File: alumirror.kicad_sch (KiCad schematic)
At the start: 71 parts, among them J1 USB_C_Receptacle_USB2.0_16P_2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, J2 USB_C_Receptacle_USB2.0_16P_2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, SW00 PG1350, SW01 PG1350, SW02 PG1350, SW03 PG1350, SW04 PG1350, SW05 PG1350, SW10 PG1350, SW11 PG1350, SW12 PG1350, SW13 PG1350, SW14 PG1350, SW15 PG1350, SW20 PG1350, SW21 PG1350, SW22 PG1350, SW23 PG1350, SW24 PG1350, SW25 PG1350_1½U, SW30 PG1350_1½U, SW31 PG1350/SKQUCAA010, SW6 BOOT, U1 CH552T, U2 CH552T, U3 USBLC6-2P6, U4 USBLC6-2P6

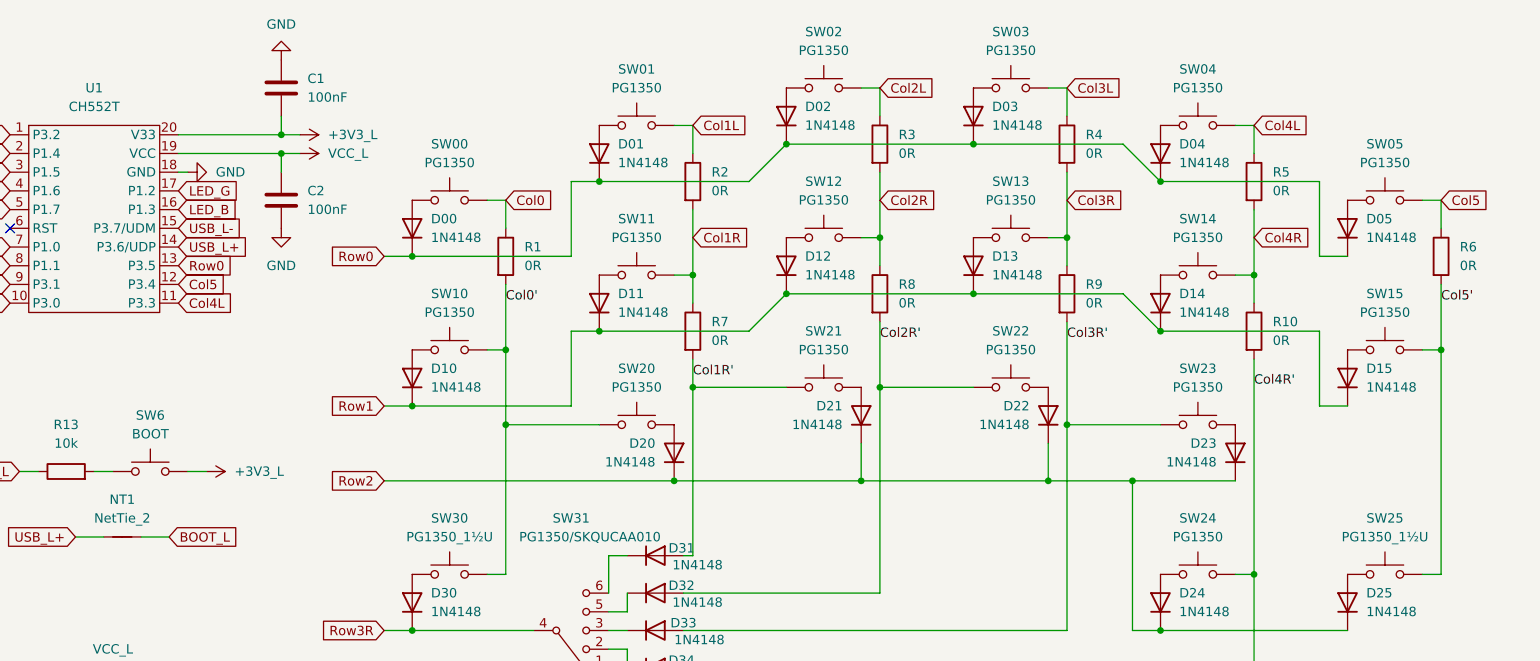
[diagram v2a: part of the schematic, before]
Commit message: Renamed all key switches to K##
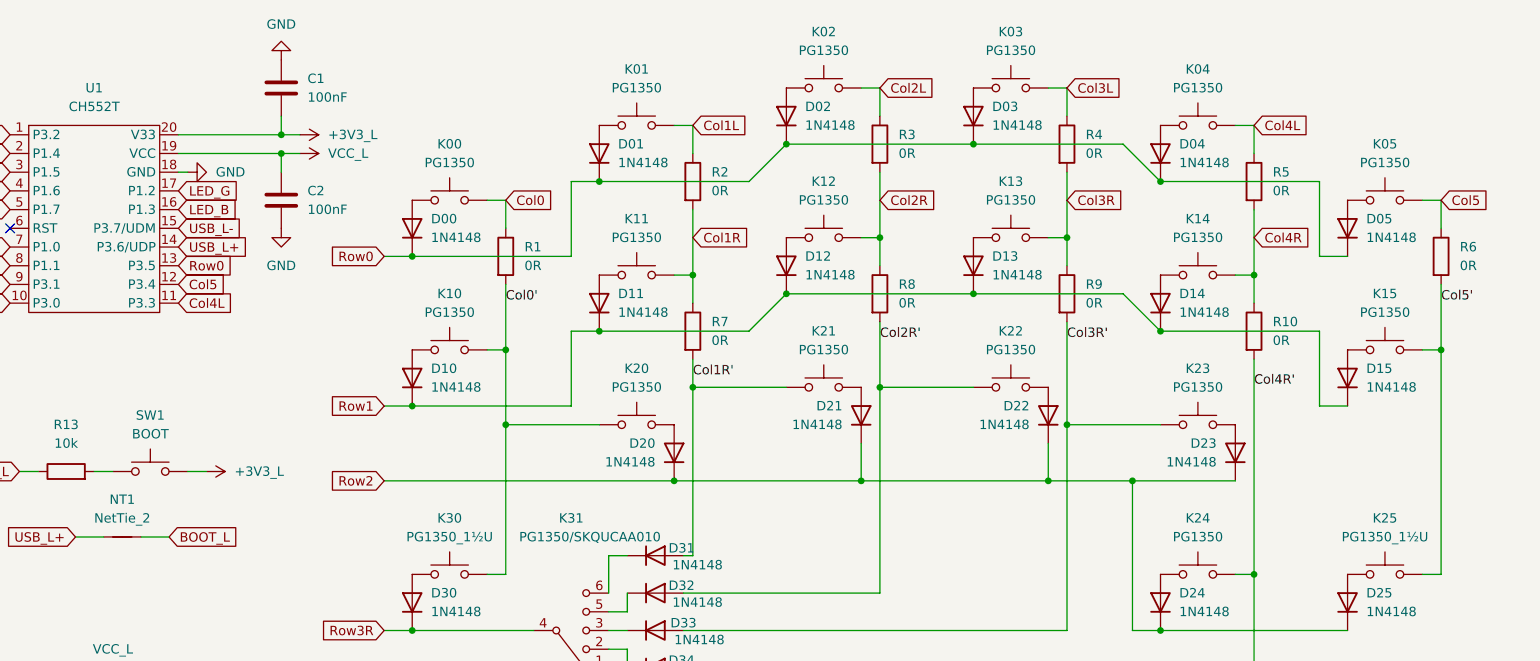
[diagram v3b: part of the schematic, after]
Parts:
- renumbered SW00 to K00, SW01 to K01, SW02 to K02, SW03 to K03, SW04 to K04, SW05 to K05, SW10 to K10, SW11 to K11, SW12 to K12, SW13 to K13, SW14 to K14, SW15 to K15, SW20 to K20, SW21 to K21, SW22 to K22, SW23 to K23, SW24 to K24, SW25 to K25, SW30 to K30, SW31 to K31, SW6 to SW1
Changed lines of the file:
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@@
 		(on_board yes)
 		(dnp no)
-		(property "Reference" "SW20"
+		(property "Reference" "K20"
 			(at 110.49 67.31 0)
 			(effects
@@
 			(project ""
 				(path "/52f043ac-ccff-4c85-bc10-2db9d3c9e3f3"
-					(reference "SW20")
+					(reference "K20")
 					(unit 1)
 				)
@@
 		(on_board yes)
 		(dnp no)
-		(property "Reference" "SW24"
+		(property "Reference" "K24"
 			(at 186.69 87.63 0)
 			(effects
@@
 			(project ""
 				(path "/52f043ac-ccff-4c85-bc10-2db9d3c9e3f3"
-					(reference "SW24")
+					(reference "K24")
 					(unit 1)
 				)
@@
 		(on_board yes)
 		(dnp no)
-		(property "Reference" "SW14"
+		(property "Reference" "K14"
 			(at 186.69 46.99 0)
 			(effects
@@
 			(project ""
 				(path "/52f043ac-ccff-4c85-bc10-2db9d3c9e3f3"
-					(reference "SW14")
+					(reference "K14")
 					(unit 1)
 				)
@@
 		(on_board yes)
 		(dnp no)
-		(property "Reference" "SW15"
+		(property "Reference" "K15"
 			(at 212.09 57.15 0)
 			(effects
@@
 			(project ""
 				(path "/52f043ac-ccff-4c85-bc10-2db9d3c9e3f3"
-					(reference "SW15")
+					(reference "K15")
 					(unit 1)
 				)
@@
 		(on_board yes)
 		(dnp no)
-		(property "Reference" "SW00"
+		(property "Reference" "K00"
 			(at 85.09 36.83 0)
 			(effects
@@
 			(project ""
 				(path "/52f043ac-ccff-4c85-bc10-2db9d3c9e3f3"
-					(reference "SW00")
+					(reference "K00")
 					(unit 1)
 				)
@@
 		(on_board yes)
 		(dnp no)
-		(property "Reference" "SW01"
+		(property "Reference" "K01"
 			(at 110.49 26.67 0)
 			(effects
@@
 			(project ""
 				(path "/52f043ac-ccff-4c85-bc10-2db9d3c9e3f3"
-					(reference "SW01")
+					(reference "K01")
 					(unit 1)
 				)
@@
 		(on_board yes)
 		(dnp no)
-		(property "Reference" "SW03"
+		(property "Reference" "K03"
 			(at 161.29 21.59 0)
 			(effects
@@
 			(project ""
 				(path "/52f043ac-ccff-4c85-bc10-2db9d3c9e3f3"
-					(reference "SW03")
+					(reference "K03")
 					(unit 1)
 				)
@@
 		(on_board yes)
 		(dnp no)
-		(property "Reference" "SW05"
+		(property "Reference" "K05"
 			(at 212.09 36.83 0)
 			(effects
@@
 			(project ""
 				(path "/52f043ac-ccff-4c85-bc10-2db9d3c9e3f3"
-					(reference "SW05")
+					(reference "K05")
 					(unit 1)
 				)
@@
 		(on_board yes)
 		(dnp no)
-		(property "Reference" "SW02"
+		(property "Reference" "K02"
 			(at 135.89 21.59 0)
 			(effects
@@
 			(project ""
 				(path "/52f043ac-ccff-4c85-bc10-2db9d3c9e3f3"
-					(reference "SW02")
+					(reference "K02")
 					(unit 1)
 				)
@@
 		(dnp no)
 		(fields_autoplaced yes)
-		(property "Reference" "SW6"
+		(property "Reference" "SW1"
 			(at 44.45 73.66 0)
 			(effects
@@
 			(project "alumirror"
 				(path "/52f043ac-ccff-4c85-bc10-2db9d3c9e3f3"
-					(reference "SW6")
+					(reference "SW1")
 					(unit 1)
 				)
@@
 		(on_board yes)
 		(dnp no)
-		(property "Reference" "SW31"
+		(property "Reference" "K31"
 			(at 101.6 87.63 0)
 			(effects
@@
 			(project ""
 				(path "/52f043ac-ccff-4c85-bc10-2db9d3c9e3f3"
-					(reference "SW31")
+					(reference "K31")
 					(unit 1)
 				)
@@
 		(on_board yes)
 		(dnp no)
-		(property "Reference" "SW12"
+		(property "Reference" "K12"
 			(at 135.89 41.91 0)
 			(effects
@@
 			(project ""
 				(path "/52f043ac-ccff-4c85-bc10-2db9d3c9e3f3"
-					(reference "SW12")
+					(reference "K12")
 					(unit 1)
 				)
@@
 		(on_board yes)
 		(dnp no)
-		(property "Reference" "SW13"
+		(property "Reference" "K13"
 			(at 161.29 41.91 0)
 			(effects
@@
 			(project ""
 				(path "/52f043ac-ccff-4c85-bc10-2db9d3c9e3f3"
-					(reference "SW13")
+					(reference "K13")
 					(unit 1)
 				)
@@
 		(on_board yes)
 		(dnp no)
-		(property "Reference" "SW25"
+		(property "Reference" "K25"
 			(at 212.09 87.63 0)
 			(effects
@@
 			(project ""
 				(path "/52f043ac-ccff-4c85-bc10-2db9d3c9e3f3"
-					(reference "SW25")
+					(reference "K25")
 					(unit 1)
 				)
@@
 		(on_board yes)
 		(dnp no)
-		(property "Reference" "SW11"
+		(property "Reference" "K11"
 			(at 110.49 46.99 0)
 			(effects
@@
 			(project ""
 				(path "/52f043ac-ccff-4c85-bc10-2db9d3c9e3f3"
-					(reference "SW11")
+					(reference "K11")
 					(unit 1)
 				)
@@
 		(on_board yes)
 		(dnp no)
-		(property "Reference" "SW30"
+		(property "Reference" "K30"
 			(at 85.09 87.63 0)
 			(effects
@@
 			(project ""
 				(path "/52f043ac-ccff-4c85-bc10-2db9d3c9e3f3"
-					(reference "SW30")
+					(reference "K30")
 					(unit 1)
 				)
@@
 		(on_board yes)
 		(dnp no)
-		(property "Reference" "SW23"
+		(property "Reference" "K23"
 			(at 186.69 67.31 0)
 			(effects
@@
 			(project ""
 				(path "/52f043ac-ccff-4c85-bc10-2db9d3c9e3f3"
-					(reference "SW23")
+					(reference "K23")
 					(unit 1)
 				)
@@
 		(on_board yes)
 		(dnp no)
-		(property "Reference" "SW04"
+		(property "Reference" "K04"
 			(at 186.69 26.67 0)
 			(effects
@@
 			(project ""
 				(path "/52f043ac-ccff-4c85-bc10-2db9d3c9e3f3"
-					(reference "SW04")
+					(reference "K04")
 					(unit 1)
 				)
@@
 		(on_board yes)
 		(dnp no)
-		(property "Reference" "SW21"
+		(property "Reference" "K21"
 			(at 135.89 62.23 0)
 			(effects
@@
 			(project ""
 				(path "/52f043ac-ccff-4c85-bc10-2db9d3c9e3f3"
-					(reference "SW21")
+					(reference "K21")
 					(unit 1)
 				)
@@
 		(on_board yes)
 		(dnp no)
-		(property "Reference" "SW10"
+		(property "Reference" "K10"
 			(at 85.09 57.15 0)
 			(effects
@@
 			(project ""
 				(path "/52f043ac-ccff-4c85-bc10-2db9d3c9e3f3"
-					(reference "SW10")
+					(reference "K10")
 					(unit 1)
 				)
@@
 		(on_board yes)
 		(dnp no)
-		(property "Reference" "SW22"
+		(property "Reference" "K22"
 			(at 161.29 62.23 0)
 			(effects
@@
 			(project ""
 				(path "/52f043ac-ccff-4c85-bc10-2db9d3c9e3f3"
-					(reference "SW22")
+					(reference "K22")
 					(unit 1)
 				)

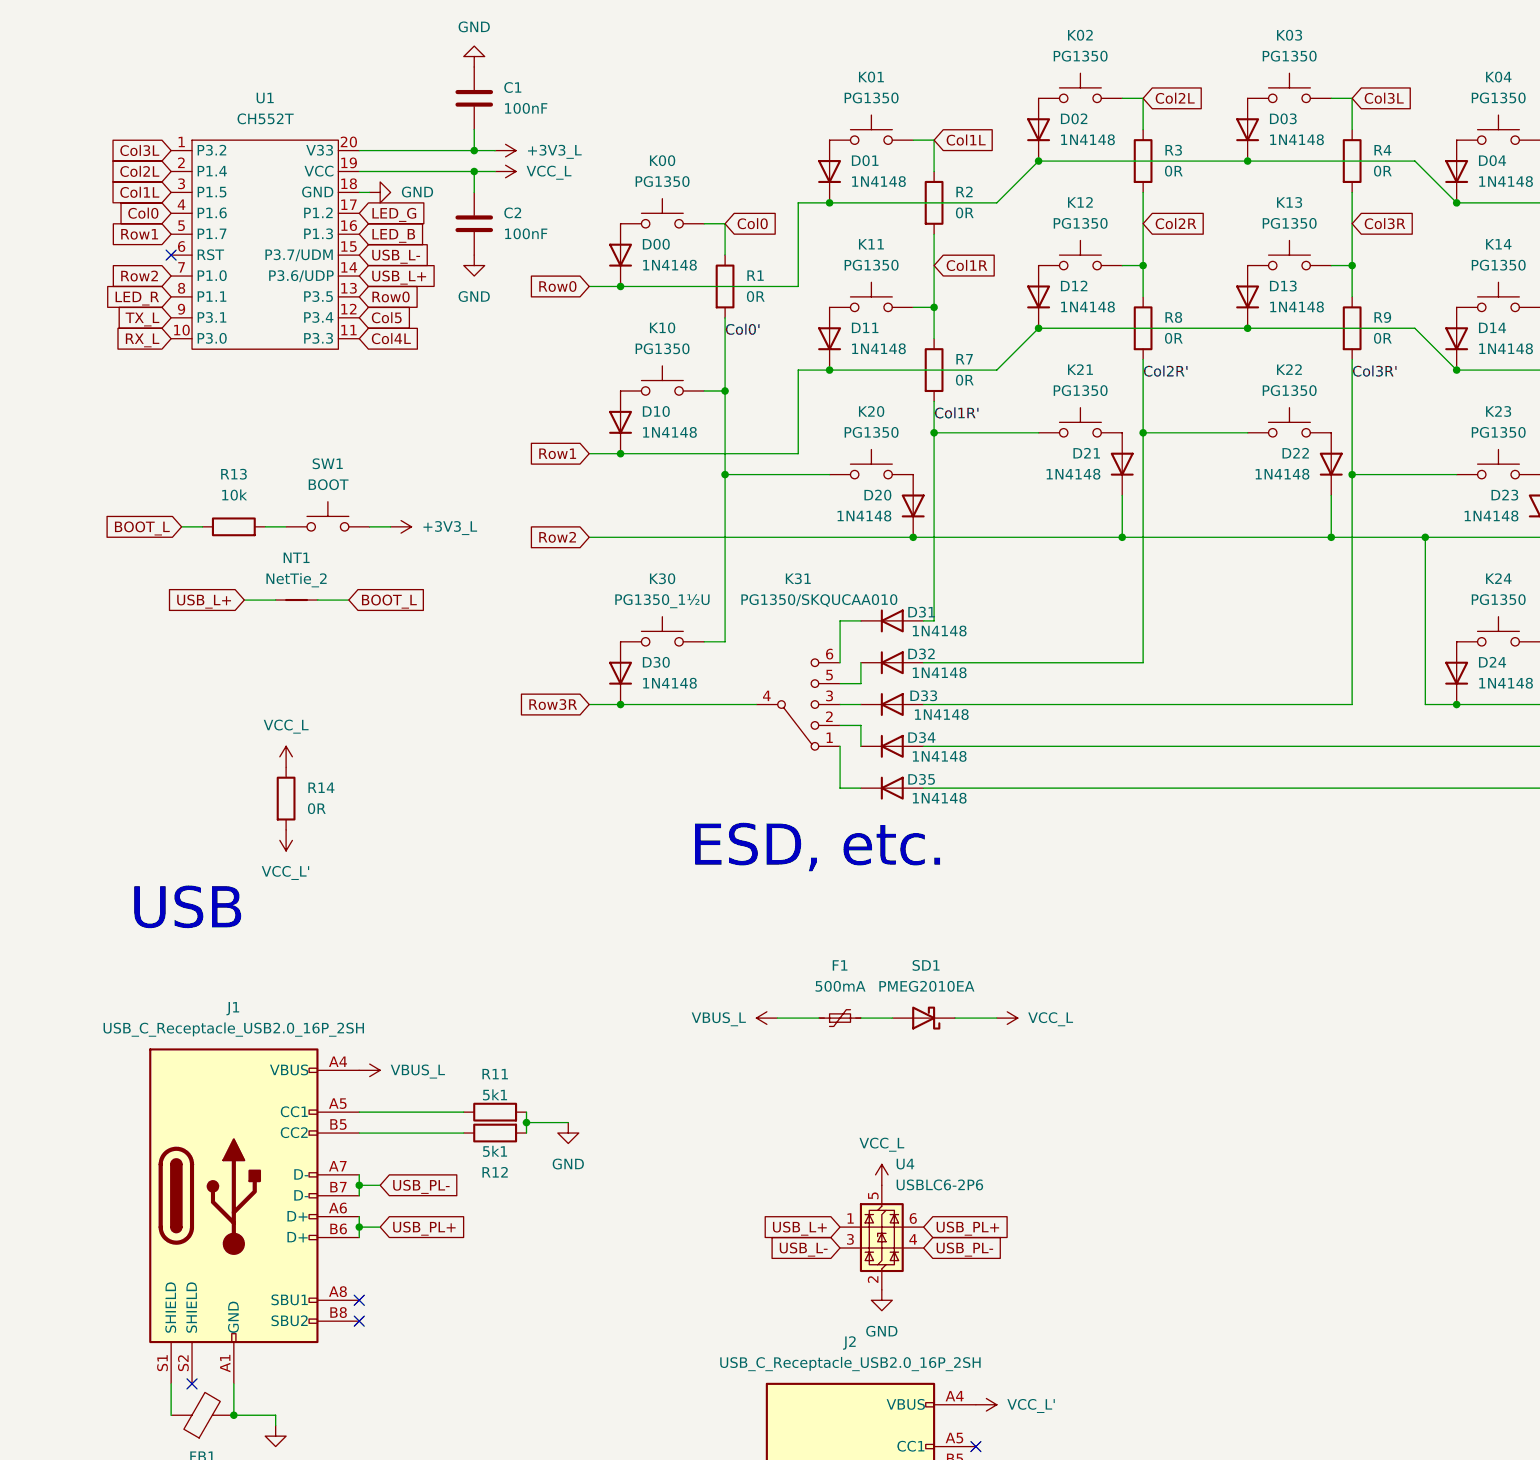
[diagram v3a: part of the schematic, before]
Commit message: Add LEDs
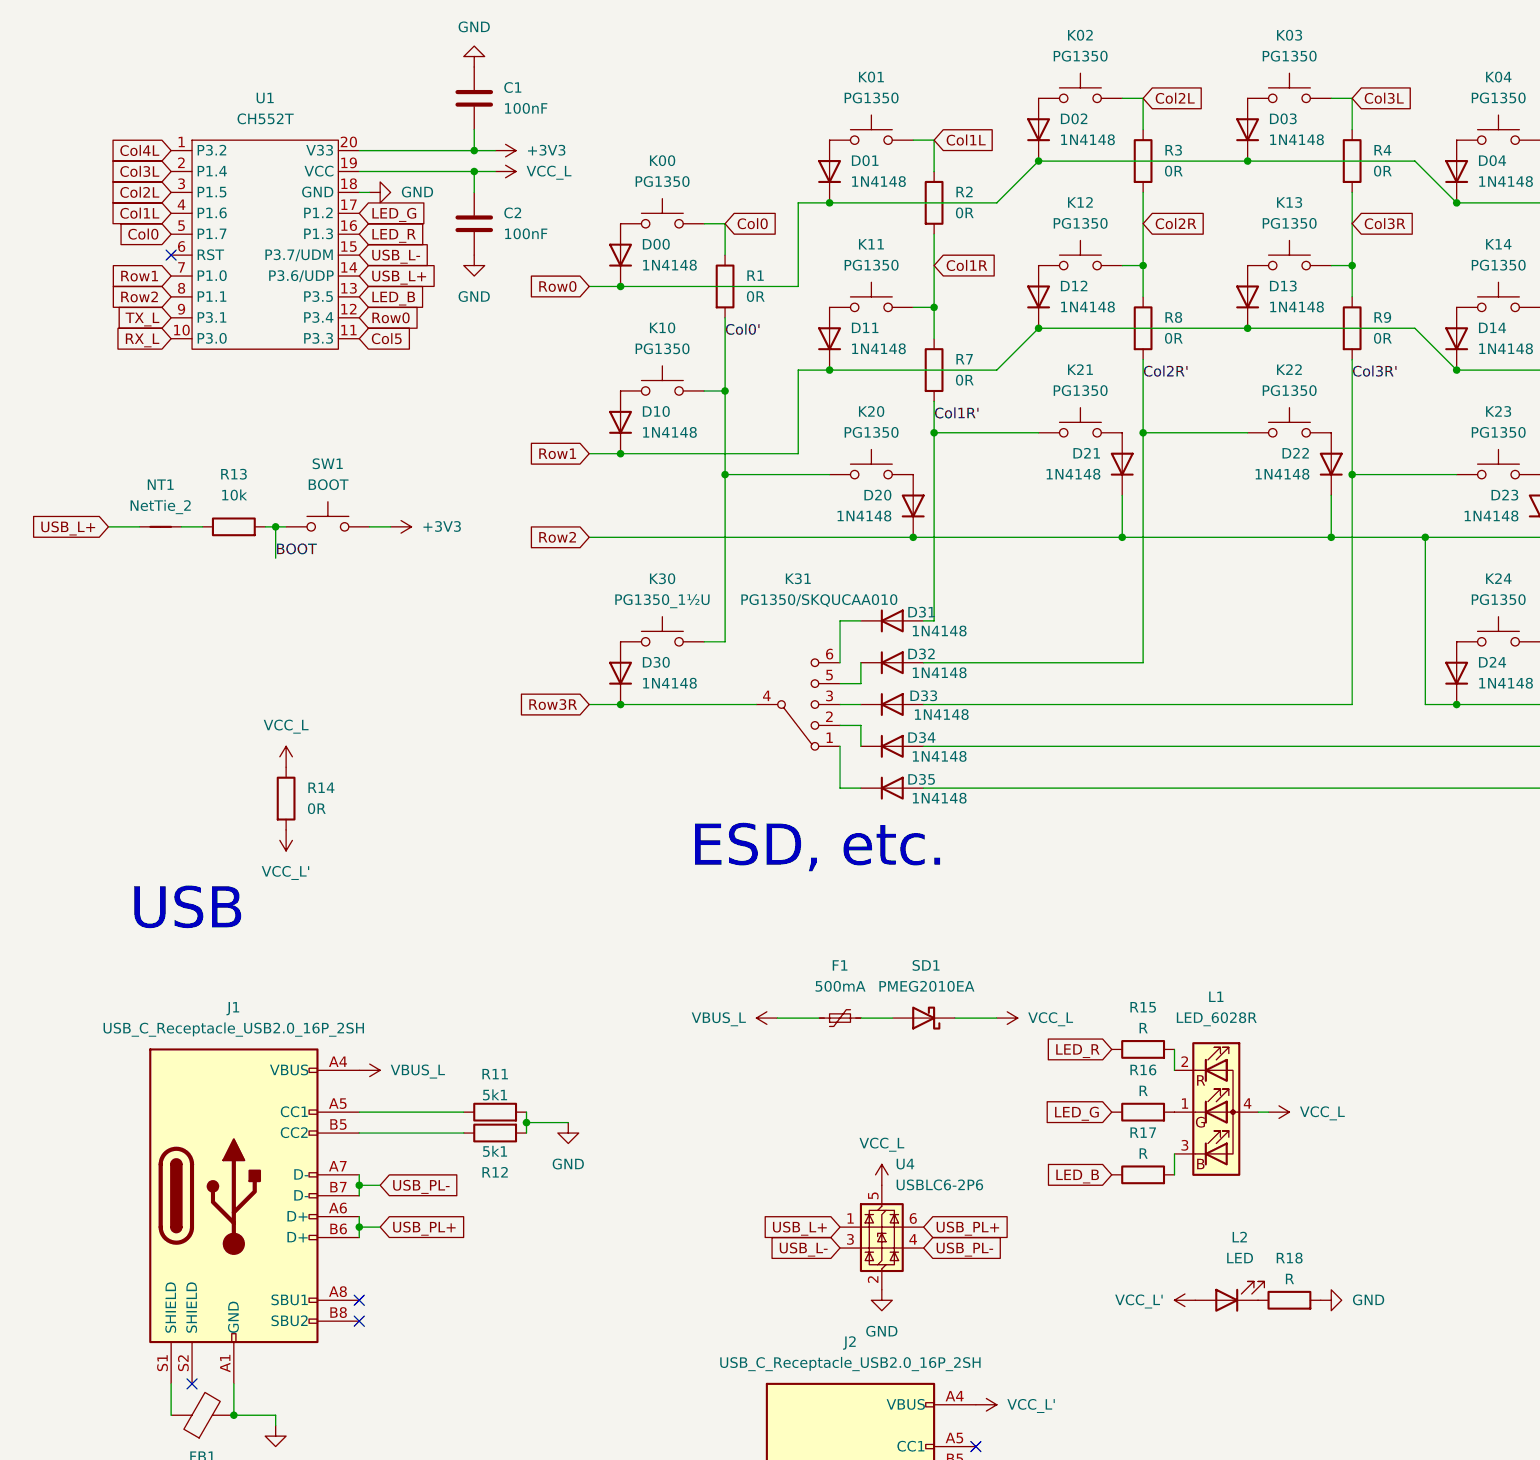
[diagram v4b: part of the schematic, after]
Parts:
- added L1: LED_6028R, PCM_marbastlib-various:LED_6028R, symbol PCM_marbastlib-various:LED_6028R
- added L2: LED, LED_SMD:LED_1206_3216Metric, symbol Device:LED
- added R15, R16, R17, R18: R, Resistor_SMD:R_0603_1608Metric, symbol Device:R
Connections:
- net Col0: now also U1.5 (P1.7); no longer U1.4 (P1.6)
- net Col1L: now also U1.4 (P1.6); no longer U1.3 (P1.5)
- net Col2L: now also U1.3 (P1.5); no longer U1.2 (P1.4)
- net Col3L: now also U1.2 (P1.4); no longer U1.1 (P3.2)
- net Col4L: now also U1.1 (P3.2); no longer U1.11 (P3.3)
- net Col5: now also U1.11 (P3.3); no longer U1.12 (P3.4)
- net GND: now also R18.2
- net LED_B: now also U1.13 (P3.5), R17.1; no longer U1.16 (P1.3)
- net LED_G: now also R16.1
- net LED_R: now also U1.16 (P1.3), R15.1; no longer U1.8 (P1.1)
- net Row0: now also U1.12 (P3.4); no longer U1.13 (P3.5)
- net Row1: now also U1.7 (P1.0); no longer U1.5 (P1.7)
- net Row2: now also U1.8 (P1.1); no longer U1.7 (P1.0)
- net VCC_L: now also L1.4 (A)
- net VCC_L': now also L2.2 (A)
- net BOOT: now reaches R13.2, SW1.1
- net +3V3_L renamed +3V3
- net BOOT_L: no longer names the net of NT1.1, R13.1
- new net: L1.3 (BK), R17.2
- new net: L2.1 (K), R18.1
- new net: L1.1 (GK), R16.2
- new net: L1.2 (RK), R15.2
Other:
- moved on the sheet: NT1

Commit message: Use smaller (0603) power LED
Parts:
- L2: footprint LED_SMD:LED_1206_3216Metric -> LED_SMD:LED_0603_1608Metric
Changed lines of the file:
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@@
 			)
 		)
-		(property "Footprint" "LED_SMD:LED_1206_3216Metric"
+		(property "Footprint" "LED_SMD:LED_0603_1608Metric"
 			(at 153.67 175.26 0)
 			(effects
